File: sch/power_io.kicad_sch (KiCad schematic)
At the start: 24 parts, among them J12 Screw_Terminal_3.5mm, J13 Conn_02x05_Odd_Even, J14 Screw_Terminal_3.5mm, J15 Screw_Terminal_3.5mm, U8 MP1584EN-LF-Z, U9 NCP1117LPST33T3G

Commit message: pcb layout update and some res package changed
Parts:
- R31: footprint Resistor_SMD:R_0603_1608Metric_Pad0.98x0.95mm_HandSolder -> Resistor_SMD:R_0402_1005Metric_Pad0.72x0.64mm_HandSolder; LCSC C25962 -> C226371
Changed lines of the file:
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@@
       (effects (font (size 1.27 1.27)) (justify left))
     )
-    (property "Footprint" "Resistor_SMD:R_0603_1608Metric_Pad0.98x0.95mm_HandSolder" (id 2) (at 169.418 83.82 90)
+    (property "Footprint" "Resistor_SMD:R_0402_1005Metric_Pad0.72x0.64mm_HandSolder" (id 2) (at 169.418 83.82 90)
       (effects (font (size 1.27 1.27)) hide)
     )
@@
       (effects (font (size 1.27 1.27)) hide)
     )
-    (property "LCSC" "C25962" (id 4) (at 167.64 83.82 0)
+    (property "LCSC" "C226371" (id 4) (at 167.64 83.82 0)
       (effects (font (size 1.27 1.27)) hide)
     )

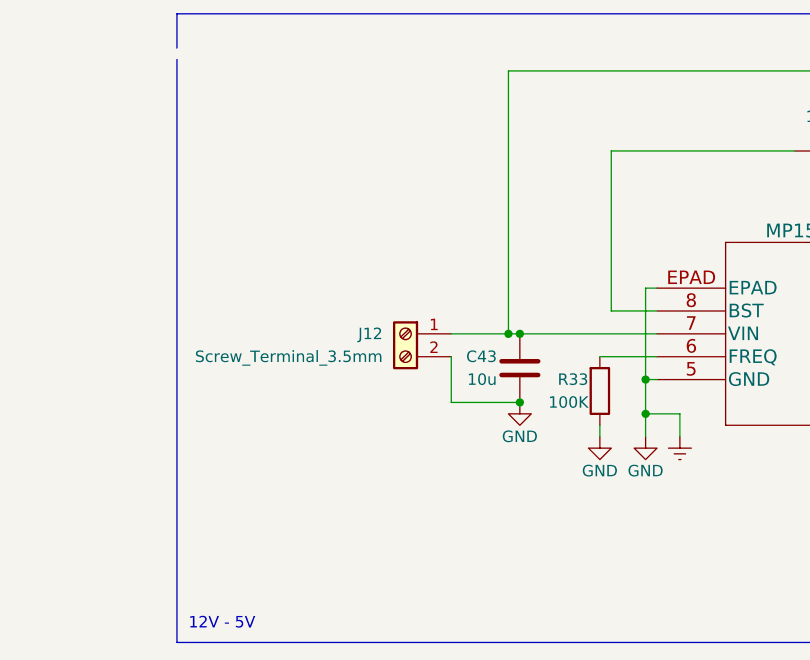
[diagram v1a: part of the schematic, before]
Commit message: wrong wiring fixed on usb switch; update layout
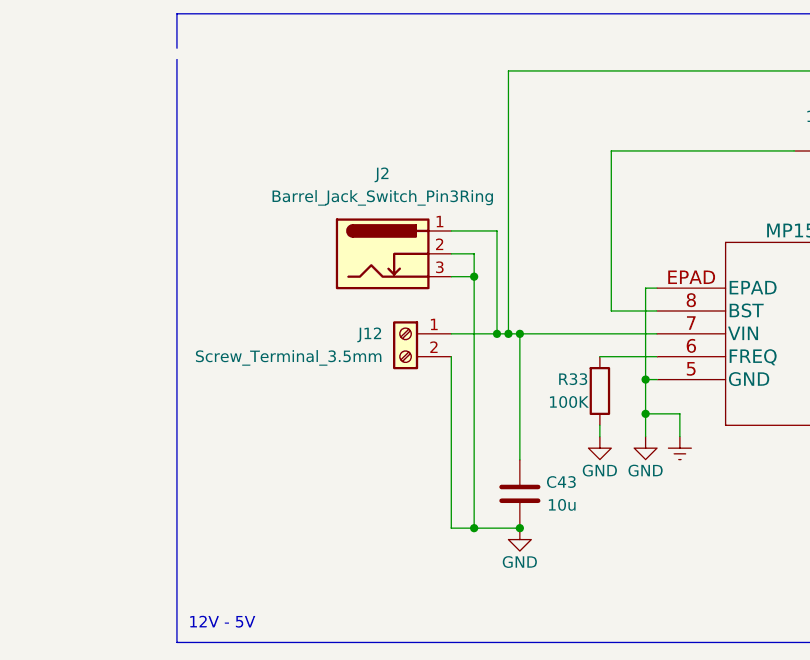
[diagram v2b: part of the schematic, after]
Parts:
- added J2: Barrel_Jack_Switch_Pin3Ring, usb_xwitch:BarrelJack_SCD556DCS113BM3G, symbol Connector:Barrel_Jack_Switch_Pin3Ring
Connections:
- net Earth: now also J2.2, J2.3
- net at C43.1, J12.1 (Pin_1), R30.2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: now also J2.1
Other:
- moved on the sheet: C43
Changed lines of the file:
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@@
     (comment 1 "Runnan Li")
   )
+  (junction (at 99.06 121.92) (diameter 0) (color 0 0 0 0)
+  )
+  (junction (at 99.06 93.98) (diameter 0) (color 0 0 0 0)
+  )
   (junction (at 191.77 95.25) (diameter 0) (color 0 0 0 0)
   )
@@
   (junction (at 182.88 95.25) (diameter 0) (color 0 0 0 0)
   )
-  (junction (at 104.14 107.95) (diameter 0) (color 0 0 0 0)
+  (junction (at 104.14 121.92) (diameter 0) (color 0 0 0 0)
   )
   (junction (at 91.44 43.18) (diameter 0) (color 0 0 0 0)
+  )
+  (junction (at 101.6 100.33) (diameter 0) (color 0 0 0 0)
   )
   (junction (at 118.11 105.41) (diameter 0) (color 0 0 0 0)
@@
     (stroke (width 0) (type default) (color 0 0 0 0))
   )
+  (wire (pts (xy 101.6 100.33) (xy 102.87 100.33))
+    (stroke (width 0) (type default) (color 0 0 0 0))
+  )
   (wire (pts (xy 124.46 41.91) (xy 124.46 43.18))
     (stroke (width 0) (type default) (color 0 0 0 0))
@@
     (stroke (width 0) (type default) (color 0 0 0 0))
   )
+  (wire (pts (xy 99.06 91.44) (xy 99.06 93.98))
+    (stroke (width 0) (type default) (color 0 0 0 0))
+  )
+  (wire (pts (xy 99.06 93.98) (xy 99.06 121.92))
+    (stroke (width 0) (type default) (color 0 0 0 0))
+  )
   (wire (pts (xy 182.88 95.25) (xy 191.77 95.25))
     (stroke (width 0) (type default) (color 0 0 0 0))
@@
     (stroke (width 0) (type default) (color 0 0 0 0))
   )
+  (wire (pts (xy 104.14 114.3) (xy 104.14 100.33))
+    (stroke (width 0) (type default) (color 0 0 0 0))
+  )
   (wire (pts (xy 113.03 110.49) (xy 113.03 111.76))
     (stroke (width 0) (type default) (color 0 0 0 0))
   )
+  (wire (pts (xy 99.06 121.92) (xy 104.14 121.92))
+    (stroke (width 0) (type default) (color 0 0 0 0))
+  )
   (wire (pts (xy 191.77 118.11) (xy 191.77 119.38))
     (stroke (width 0) (type default) (color 0 0 0 0))
@@
     (stroke (width 0) (type default) (color 0 0 0 0))
   )
+  (wire (pts (xy 96.52 88.9) (xy 101.6 88.9))
+    (stroke (width 0) (type default) (color 0 0 0 0))
+  )
   (wire (pts (xy 191.77 109.22) (xy 191.77 110.49))
     (stroke (width 0) (type default) (color 0 0 0 0))
@@
     (stroke (width 0) (type default) (color 0 0 0 0))
   )
-  (wire (pts (xy 96.52 107.95) (xy 104.14 107.95))
+  (wire (pts (xy 96.52 121.92) (xy 99.06 121.92))
     (stroke (width 0) (type default) (color 0 0 0 0))
   )
@@
     (stroke (width 0) (type default) (color 0 0 0 0))
   )
-  (wire (pts (xy 96.52 102.87) (xy 96.52 107.95))
+  (wire (pts (xy 96.52 91.44) (xy 99.06 91.44))
+    (stroke (width 0) (type default) (color 0 0 0 0))
+  )
+  (wire (pts (xy 96.52 102.87) (xy 96.52 121.92))
     (stroke (width 0) (type default) (color 0 0 0 0))
   )
@@
     (stroke (width 0) (type default) (color 0 0 0 0))
   )
+  (wire (pts (xy 101.6 88.9) (xy 101.6 100.33))
+    (stroke (width 0) (type default) (color 0 0 0 0))
+  )
   (wire (pts (xy 104.14 53.34) (xy 78.74 53.34))
     (stroke (width 0) (type default) (color 0 0 0 0))
@@
     (stroke (width 0) (type default) (color 0 0 0 0))
   )
+  (wire (pts (xy 96.52 93.98) (xy 99.06 93.98))
+    (stroke (width 0) (type default) (color 0 0 0 0))
+  )
   (polyline (pts (xy 66.04 69.85) (xy 66.04 134.62))
     (stroke (width 0) (type default) (color 0 0 0 0))
@@
     (stroke (width 0) (type default) (color 0 0 0 0))
   )
-  (wire (pts (xy 96.52 100.33) (xy 102.87 100.33))
+  (wire (pts (xy 96.52 100.33) (xy 101.6 100.33))
     (stroke (width 0) (type default) (color 0 0 0 0))
   )
@@
     (pin "2")
   )
-  (symbol (lib_id "Device:C") (at 104.14 104.14 0) (mirror y) (unit 1)
-    (in_bom yes) (on_board yes)
-    (property "Reference" "C43" (id 0) (at 101.6 102.87 0)
-      (effects (font (size 1.27 1.27)) (justify left))
-    )
-    (property "Value" "10u" (id 1) (at 101.6 105.41 0)
-      (effects (font (size 1.27 1.27)) (justify left))
-    )
-    (property "Footprint" "Capacitor_SMD:C_0805_2012Metric_Pad1.18x1.45mm_HandSolder" (id 2) (at 103.1748 107.95 0)
-      (effects (font (size 1.27 1.27)) hide)
-    )
-    (property "Datasheet" "~" (id 3) (at 104.14 104.14 0)
-      (effects (font (size 1.27 1.27)) hide)
-    )
-    (property "LCSC" "C440198" (id 4) (at 104.14 104.14 0)
+  (symbol (lib_id "Device:C") (at 104.14 118.11 0) (mirror y) (unit 1)
+    (in_bom yes) (on_board yes)
+    (property "Reference" "C43" (id 0) (at 110.49 116.84 0)
+      (effects (font (size 1.27 1.27)) (justify left))
+    )
+    (property "Value" "10u" (id 1) (at 110.49 119.38 0)
+      (effects (font (size 1.27 1.27)) (justify left))
+    )
+    (property "Footprint" "Capacitor_SMD:C_0805_2012Metric_Pad1.18x1.45mm_HandSolder" (id 2) (at 103.1748 121.92 0)
+      (effects (font (size 1.27 1.27)) hide)
+    )
+    (property "Datasheet" "~" (id 3) (at 104.14 118.11 0)
+      (effects (font (size 1.27 1.27)) hide)
+    )
+    (property "LCSC" "C440198" (id 4) (at 104.14 118.11 0)
       (effects (font (size 1.27 1.27)) hide)
     )
@@
     (pin "1")
   )
+  (symbol (lib_id "Connector:Barrel_Jack_Switch_Pin3Ring") (at 88.9 91.44 0) (unit 1)
+    (in_bom yes) (on_board yes) (fields_autoplaced)
+    (property "Reference" "J2" (id 0) (at 88.9 82.55 0))
+    (property "Value" "Barrel_Jack_Switch_Pin3Ring" (id 1) (at 88.9 85.09 0))
+    (property "Footprint" "usb_xwitch:BarrelJack_SCD556DCS113BM3G" (id 2) (at 90.17 92.456 0)
+      (effects (font (size 1.27 1.27)) hide)
+    )
+    (property "Datasheet" "~" (id 3) (at 90.17 92.456 0)
+      (effects (font (size 1.27 1.27)) hide)
+    )
+    (pin "1")
+    (pin "2")
+    (pin "3")
+  )
   (symbol (lib_id "power:GND") (at 39.37 46.99 0) (unit 1)
     (in_bom yes) (on_board yes)
@@
     (pin "2")
   )
-  (symbol (lib_id "power:GND") (at 104.14 107.95 0) (mirror y) (unit 1)
-    (in_bom yes) (on_board yes)
-    (property "Reference" "#PWR0114" (id 0) (at 104.14 114.3 0)
-      (effects (font (size 1.27 1.27)) hide)
-    )
-    (property "Value" "GND" (id 1) (at 104.14 111.76 0))
-    (property "Footprint" "" (id 2) (at 104.14 107.95 0)
-      (effects (font (size 1.27 1.27)) hide)
-    )
-    (property "Datasheet" "" (id 3) (at 104.14 107.95 0)
-      (effects (font (size 1.27 1.27)) hide)
-    )
+  (symbol (lib_id "power:GND") (at 104.14 121.92 0) (mirror y) (unit 1)
+    (in_bom yes) (on_board yes)
+    (property "Reference" "#PWR0114" (id 0) (at 104.14 128.27 0)
+      (effects (font (size 1.27 1.27)) hide)
+    )
+    (property "Value" "GND" (id 1) (at 104.14 125.73 0))
+    (property "Footprint" "" (id 2) (at 104.14 121.92 0)
+      (effects (font (size 1.27 1.27)) hide)
+    )
+    (property "Datasheet" "" (id 3) (at 104.14 121.92 0)
+      (effects (font (size 1.27 1.27)) hide)
+    )

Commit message: routing power area
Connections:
- net PWR_IN: now reaches C43.1, J12.1 (Pin_1), J2.1, R30.2, U8.7 (VIN)
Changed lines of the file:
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@@
     (effects (font (size 1.27 1.27)) (justify right bottom))
+  )
+  (label "PWR_IN" (at 105.41 100.33 0)
+    (effects (font (size 1.27 1.27)) (justify left bottom))
   )
   (label "UART_TX_UP" (at 245.11 40.64 180)
